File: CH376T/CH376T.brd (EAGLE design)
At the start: 24.1 x 30.5 mm, 14 parts

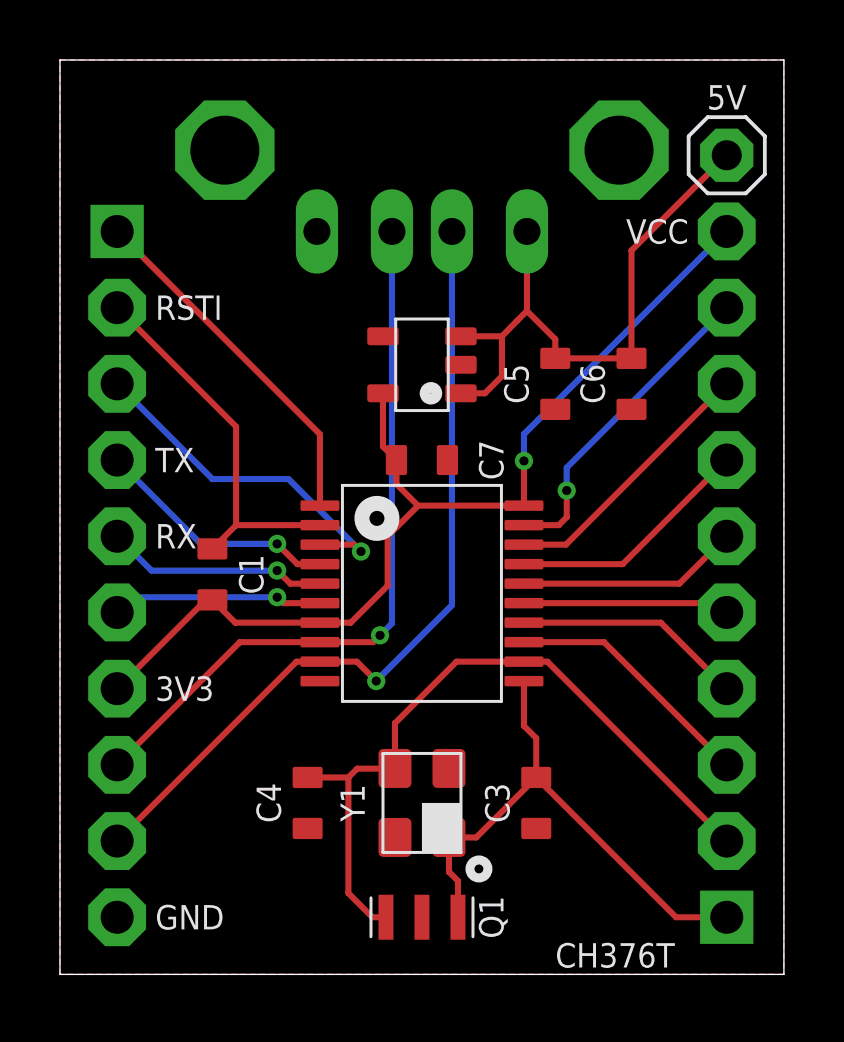
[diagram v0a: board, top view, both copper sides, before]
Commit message: add resister
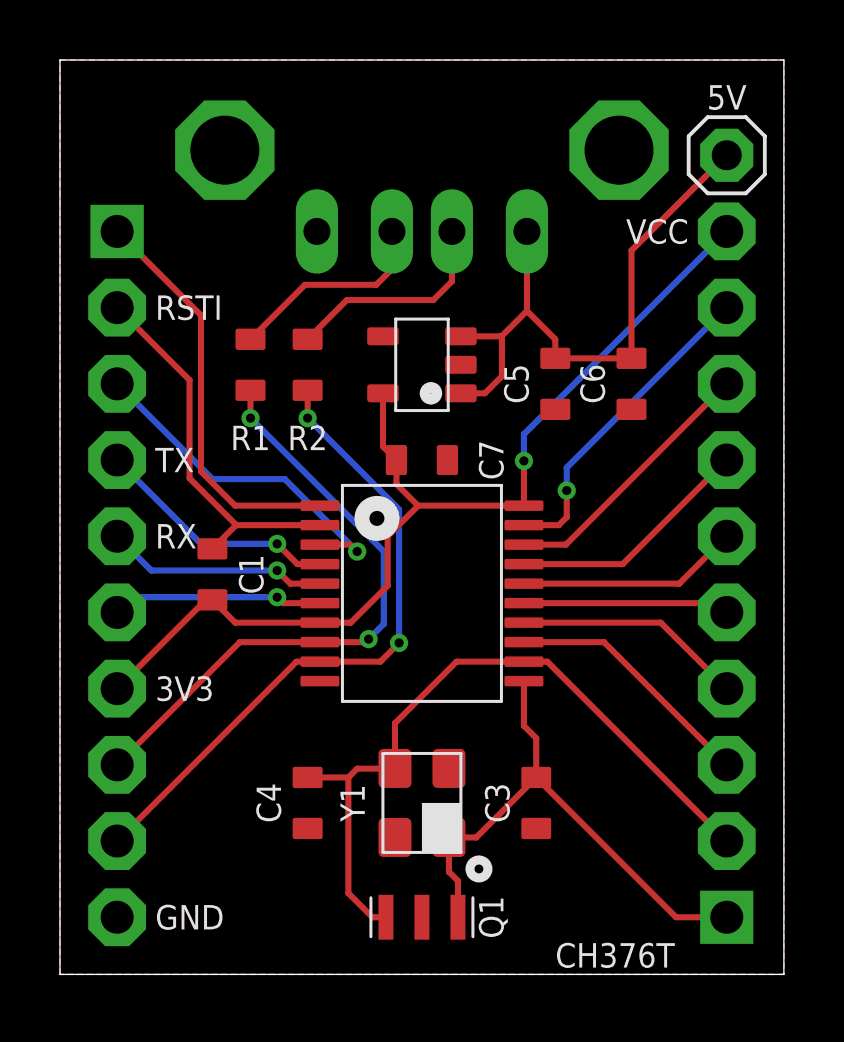
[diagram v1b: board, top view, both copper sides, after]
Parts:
- added R1, R2: 2, FaBo-Resistors:0603-NARROW
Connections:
- new net N$1: R1.1, USB1.3
- new net N$2: R2.1, USB1.2
- net DM: now also R2.2; no longer USB1.2
- net DP: now also R1.2; no longer USB1.3
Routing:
- net N$2: track 0.00 -> 7.28 mm
- net N$1: track 0.00 -> 6.94 mm
- net DM: track 27.4 -> 21.8 mm, vias 1 -> 2
- net DP: track 24.2 -> 20.5 mm, vias 1 -> 2
- net INT: track 11.9 -> 13.6 mm
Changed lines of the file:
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@@
 <element name="CN2" library="FaBo-PIN" package="PIN_1X10" value="" x="22.225" y="13.335" smashed="yes" rot="R90"/>
 <element name="CN3" library="FaBo-PIN" package="PIN_1X1" value="" x="22.225" y="27.305" smashed="yes"/>
+<element name="R1" library="FaBo-Resistors" package="0603-NARROW" value="2" x="6.35" y="20.32" smashed="yes" rot="R270">
+<attribute name="NAME" x="6.35" y="18.288" size="0.8128" layer="25" font="vector" ratio="12" rot="R180" align="bottom-center"/>
+<attribute name="VALUE" x="6.35" y="20.32" size="0.8128" layer="27" font="vector" ratio="12" rot="R270" align="center"/>
+</element>
+<element name="R2" library="FaBo-Resistors" package="0603-NARROW" value="2" x="8.255" y="20.32" smashed="yes" rot="R270">
+<attribute name="NAME" x="8.255" y="18.288" size="0.8128" layer="25" font="vector" ratio="12" rot="R180" align="bottom-center"/>
+<attribute name="VALUE" x="8.255" y="20.32" size="0.8128" layer="27" font="vector" ratio="12" rot="R270" align="center"/>
+</element>
 </elements>
 <signals>
@@
 <wire x1="8.665" y1="14.975" x2="5.87" y2="14.975" width="0.2032" layer="1"/>
 <wire x1="5.87" y1="14.975" x2="5.08" y2="14.185" width="0.2032" layer="1"/>
-<wire x1="5.87" y1="14.975" x2="5.87" y2="18.26" width="0.2032" layer="1"/>
-<wire x1="5.87" y1="18.26" x2="1.905" y2="22.225" width="0.2032" layer="1"/>
+<wire x1="5.87" y1="14.975" x2="5.87" y2="14.986" width="0.2032" layer="1"/>
+<wire x1="1.905" y1="22.225" x2="4.318" y2="19.812" width="0.2032" layer="1"/>
+<wire x1="4.318" y1="19.812" x2="4.318" y2="16.538" width="0.2032" layer="1"/>
+<wire x1="4.318" y1="16.538" x2="5.87" y2="14.986" width="0.2032" layer="1"/>
 </signal>
 <signal name="TX">
@@
 <contactref element="USB1" pad="1"/>
 <wire x1="19.05" y1="20.535" x2="16.51" y2="20.535" width="0.2032" layer="1"/>
-<wire x1="13.365" y1="21.27" x2="14.732" y2="21.27" width="0.2032" layer="1"/>
-<wire x1="14.732" y1="21.27" x2="15.228" y2="21.778" width="0.2032" layer="1"/>
 <wire x1="13.365" y1="19.37" x2="14.163" y2="19.37" width="0.2032" layer="1"/>
 <wire x1="14.163" y1="19.37" x2="14.732" y2="19.939" width="0.2032" layer="1"/>
-<wire x1="14.732" y1="19.939" x2="14.732" y2="21.27" width="0.2032" layer="1"/>
+<wire x1="14.732" y1="19.939" x2="14.732" y2="21.209" width="0.2032" layer="1"/>
 <contactref element="CN3" pad="1"/>
+<wire x1="14.732" y1="21.209" x2="14.732" y2="21.282" width="0.2032" layer="1"/>
 <wire x1="19.05" y1="20.535" x2="19.05" y2="24.13" width="0.2032" layer="1"/>
 <wire x1="19.05" y1="24.13" x2="22.225" y2="27.305" width="0.2032" layer="1"/>
 <wire x1="15.565" y1="24.765" x2="15.565" y2="22.115" width="0.2032" layer="1"/>
-<wire x1="15.565" y1="22.115" x2="15.228" y2="21.778" width="0.2032" layer="1"/>
 <wire x1="16.51" y1="20.535" x2="16.51" y2="21.17" width="0.2032" layer="1"/>
 <wire x1="16.51" y1="21.17" x2="15.565" y2="22.115" width="0.2032" layer="1"/>
+<wire x1="14.732" y1="21.282" x2="15.565" y2="22.115" width="0.2032" layer="1"/>
+<wire x1="13.365" y1="21.27" x2="14.671" y2="21.27" width="0.2032" layer="1"/>
+<wire x1="14.671" y1="21.27" x2="14.732" y2="21.209" width="0.2032" layer="1"/>
 </signal>
 <signal name="DP">
-<contactref element="USB1" pad="3"/>
 <contactref element="IC2" pad="8"/>
 <contactref element="CN1" pad="8"/>
 <wire x1="8.665" y1="11.075" x2="5.995" y2="11.075" width="0.2032" layer="1"/>
 <wire x1="5.995" y1="11.075" x2="1.905" y2="6.985" width="0.2032" layer="1"/>
-<wire x1="8.665" y1="11.075" x2="10.44" y2="11.075" width="0.2032" layer="1"/>
-<wire x1="10.44" y1="11.075" x2="10.668" y2="11.303" width="0.2032" layer="1"/>
-<via x="10.668" y="11.303" extent="1-16" drill="0.3048"/>
-<wire x1="10.668" y1="11.303" x2="11.065" y2="11.7" width="0.2032" layer="16"/>
-<wire x1="11.065" y1="11.7" x2="11.065" y2="24.765" width="0.2032" layer="16"/>
+<contactref element="R1" pad="2"/>
+<wire x1="8.665" y1="11.075" x2="10.186" y2="11.075" width="0.2032" layer="1"/>
+<wire x1="10.186" y1="11.075" x2="10.287" y2="11.176" width="0.2032" layer="1"/>
+<via x="10.287" y="11.176" extent="1-16" drill="0.3048"/>
+<wire x1="10.287" y1="11.176" x2="10.795" y2="11.684" width="0.2032" layer="16"/>
+<wire x1="10.795" y1="11.684" x2="10.795" y2="14.097" width="0.2032" layer="16"/>
+<wire x1="10.795" y1="14.097" x2="6.35" y2="18.542" width="0.2032" layer="16"/>
+<via x="6.35" y="18.542" extent="1-16" drill="0.3048"/>
+<wire x1="6.35" y1="18.542" x2="6.35" y2="19.47" width="0.2032" layer="1"/>
 </signal>
 <signal name="DM">
-<contactref element="USB1" pad="2"/>
 <contactref element="IC2" pad="9"/>
 <contactref element="CN1" pad="9"/>
 <wire x1="8.665" y1="10.425" x2="7.885" y2="10.425" width="0.2032" layer="1"/>
 <wire x1="7.885" y1="10.425" x2="1.905" y2="4.445" width="0.2032" layer="1"/>
-<wire x1="8.665" y1="10.425" x2="9.895" y2="10.425" width="0.2032" layer="1"/>
-<wire x1="9.895" y1="10.425" x2="10.541" y2="9.779" width="0.2032" layer="1"/>
-<wire x1="13.065" y1="24.765" x2="13.065" y2="12.303" width="0.2032" layer="16"/>
-<via x="10.541" y="9.779" extent="1-16" drill="0.3048"/>
-<wire x1="13.065" y1="12.303" x2="10.541" y2="9.779" width="0.2032" layer="16"/>
+<contactref element="R2" pad="2"/>
+<wire x1="8.665" y1="10.425" x2="10.679" y2="10.425" width="0.2032" layer="1"/>
+<wire x1="10.679" y1="10.425" x2="11.303" y2="11.049" width="0.2032" layer="1"/>
+<via x="11.303" y="11.049" extent="1-16" drill="0.3048"/>
+<via x="8.255" y="18.542" extent="1-16" drill="0.3048"/>
+<wire x1="8.255" y1="18.542" x2="8.255" y2="19.47" width="0.2032" layer="1"/>
+<wire x1="8.255" y1="18.542" x2="11.303" y2="15.494" width="0.2032" layer="16"/>
+<wire x1="11.303" y1="11.049" x2="11.303" y2="15.494" width="0.2032" layer="16"/>
 </signal>
 <signal name="SCS">
@@
 <contactref element="IC2" pad="3"/>
 <contactref element="CN1" pad="3"/>
-<wire x1="8.665" y1="14.325" x2="9.805" y2="14.325" width="0.2032" layer="1"/>
-<wire x1="9.805" y1="14.325" x2="10.033" y2="14.097" width="0.2032" layer="1"/>
-<via x="10.033" y="14.097" extent="1-16" drill="0.3048"/>
-<wire x1="10.033" y1="14.097" x2="7.62" y2="16.51" width="0.2032" layer="16"/>
-<wire x1="7.62" y1="16.51" x2="5.08" y2="16.51" width="0.2032" layer="16"/>
+<wire x1="8.665" y1="14.325" x2="9.678" y2="14.325" width="0.2032" layer="1"/>
+<wire x1="9.678" y1="14.325" x2="9.906" y2="14.097" width="0.2032" layer="1"/>
+<via x="9.906" y="14.097" extent="1-16" drill="0.3048"/>
+<wire x1="9.906" y1="14.097" x2="7.493" y2="16.51" width="0.2032" layer="16"/>
+<wire x1="7.493" y1="16.51" x2="5.08" y2="16.51" width="0.2032" layer="16"/>
 <wire x1="5.08" y1="16.51" x2="1.905" y2="19.685" width="0.2032" layer="16"/>
 </signal>
@@
 <contactref element="IC2" pad="1"/>
 <contactref element="CN1" pad="1"/>
-<wire x1="8.665" y1="15.625" x2="8.665" y2="18.005" width="0.2032" layer="1"/>
-<wire x1="8.665" y1="18.005" x2="1.905" y2="24.765" width="0.2032" layer="1"/>
+<wire x1="8.665" y1="15.625" x2="5.838" y2="15.625" width="0.2032" layer="1"/>
+<wire x1="5.838" y1="15.625" x2="4.699" y2="16.764" width="0.2032" layer="1"/>
+<wire x1="4.699" y1="16.764" x2="4.699" y2="21.971" width="0.2032" layer="1"/>
+<wire x1="4.699" y1="21.971" x2="1.905" y2="24.765" width="0.2032" layer="1"/>
+</signal>
+<signal name="N$1">
+<contactref element="USB1" pad="3"/>
+<contactref element="R1" pad="1"/>
+<wire x1="11.065" y1="24.765" x2="11.065" y2="23.511" width="0.2032" layer="1"/>
+<wire x1="11.065" y1="23.511" x2="10.541" y2="22.987" width="0.2032" layer="1"/>
+<wire x1="10.541" y1="22.987" x2="8.167" y2="22.987" width="0.2032" layer="1"/>
+<wire x1="8.167" y1="22.987" x2="6.35" y2="21.17" width="0.2032" layer="1"/>
+</signal>
+<signal name="N$2">
+<contactref element="USB1" pad="2"/>
+<contactref element="R2" pad="1"/>
+<wire x1="13.065" y1="24.765" x2="13.065" y2="23.098" width="0.2032" layer="1"/>
+<wire x1="13.065" y1="23.098" x2="12.446" y2="22.479" width="0.2032" layer="1"/>
+<wire x1="12.446" y1="22.479" x2="9.564" y2="22.479" width="0.2032" layer="1"/>
+<wire x1="9.564" y1="22.479" x2="8.255" y2="21.17" width="0.2032" layer="1"/>
 </signal>
 </signals>
